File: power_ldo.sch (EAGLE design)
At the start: 7 parts

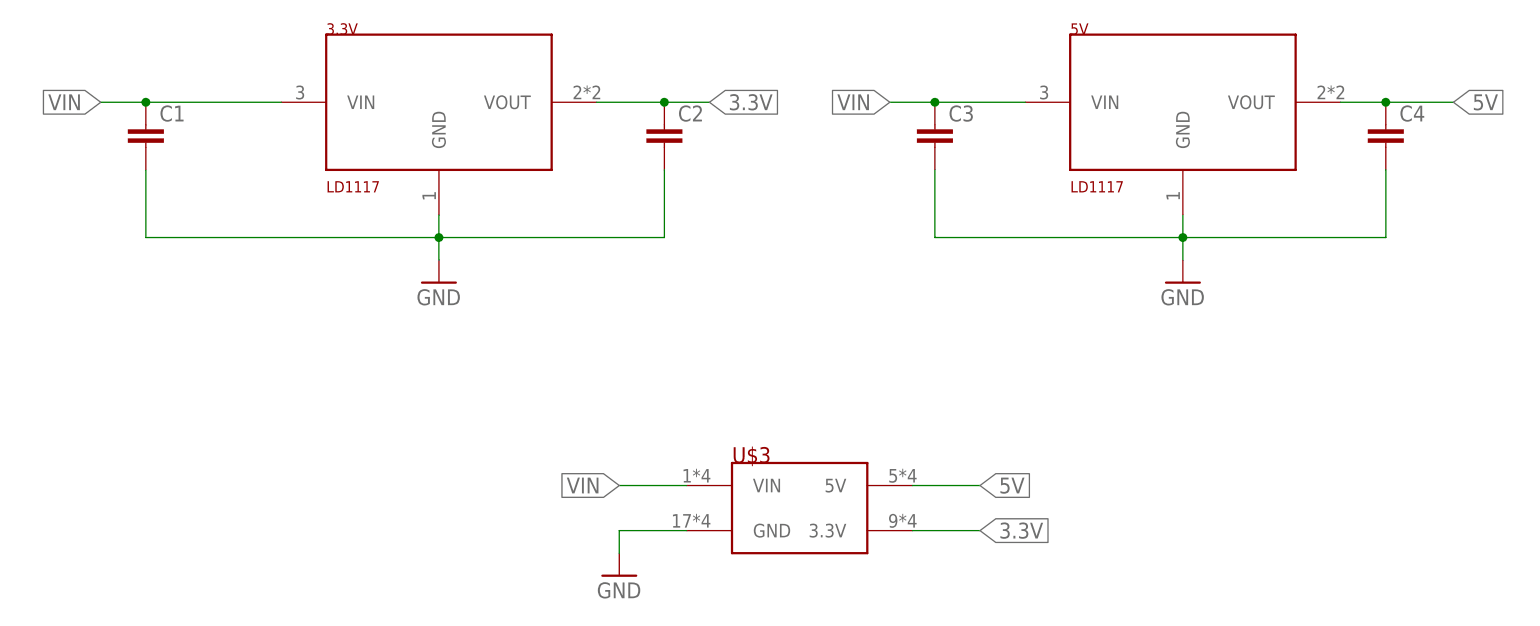
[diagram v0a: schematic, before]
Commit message: Add cap values
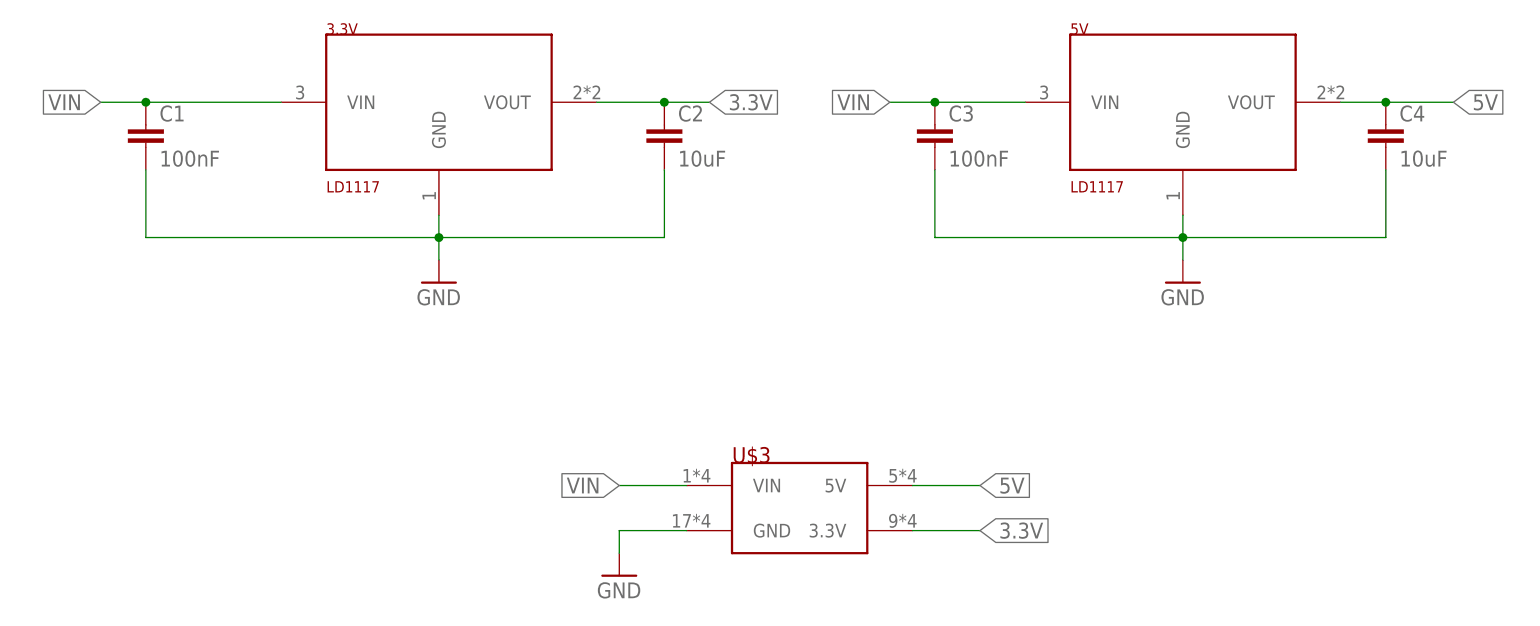
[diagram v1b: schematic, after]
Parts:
- C1, C3: value (none) -> 100nF
- C2, C4: value (none) -> 10uF
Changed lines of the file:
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@@
 <part name="U$3" library="auv" deviceset="POWER_EDGE_CONN" device="EDGE"/>
 <part name="GND1" library="auv" deviceset="GND" device=""/>
-<part name="C1" library="auv" deviceset="C-EU" device="C0603"/>
-<part name="C2" library="auv" deviceset="C-EU" device="C0603"/>
-<part name="C3" library="auv" deviceset="C-EU" device="C0603"/>
-<part name="C4" library="auv" deviceset="C-EU" device="C0603"/>
+<part name="C1" library="auv" deviceset="C-EU" device="C0603" value="100nF"/>
+<part name="C2" library="auv" deviceset="C-EU" device="C0603" value="10uF"/>
+<part name="C3" library="auv" deviceset="C-EU" device="C0603" value="100nF"/>
+<part name="C4" library="auv" deviceset="C-EU" device="C0603" value="10uF"/>
 <part name="GND2" library="auv" deviceset="GND" device=""/>
 <part name="GND3" library="auv" deviceset="GND" device=""/>
